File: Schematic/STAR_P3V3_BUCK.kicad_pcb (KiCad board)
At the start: 2 copper layers, 70.1 x 70 mm, 19 parts, among them J1 1017491, J2 6120XX21621_61200621621, J3 6120XX21621_61200821621, U1 TLV62569ADRLR

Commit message: V1.2.0
Lots Of changes, need help with screw holes
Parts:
- moved H4 12.5 mm to (190.0, 84.8)
- moved C8 10.7 mm to (171.2, 69.8), turned to -90 degrees
- moved H3 9.63 mm to (143.9, 84.8)
- moved C4 9.16 mm to (148.6, 71.0), turned to 90 degrees
- moved H2 8.99 mm to (190.0, 41.3)
- moved C7 8.58 mm to (168.4, 69.8), turned to 90 degrees
- moved J3 8.41 mm to (181.1, 72.8)
- moved R2 7.62 mm to (164.7, 64.6)
- moved C1 7.58 mm to (156.7, 71.0), turned to 90 degrees
- moved C6 5.78 mm to (173.8, 69.8), turned to 90 degrees
- moved L1 5.47 mm to (167.9, 76.4)
- moved H1 4.71 mm to (143.3, 41.3)
- moved J2 3.94 mm to (178.0, 57.5)
- moved C5 2.87 mm to (159.9, 71.0), turned to 90 degrees
- moved R1 2.30 mm to (164.7, 66.3), turned to 0 degrees
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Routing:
- net GND: track 43.8 -> 19.9 mm, vias 13 -> 12
- net /P3V3_BUCK: track 36.5 -> 22.4 mm, vias 7 -> 2
- net Net-(U1-SW): track 3.00 -> 5.57 mm
- net Net-(U1-FB): track 3.01 -> 4.44 mm
- net /P5V0_BUCK: track 13.1 -> 12.0 mm, vias 7 -> 5
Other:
- board size 70.1 x 70 mm -> 43.3 x 40.1 mm

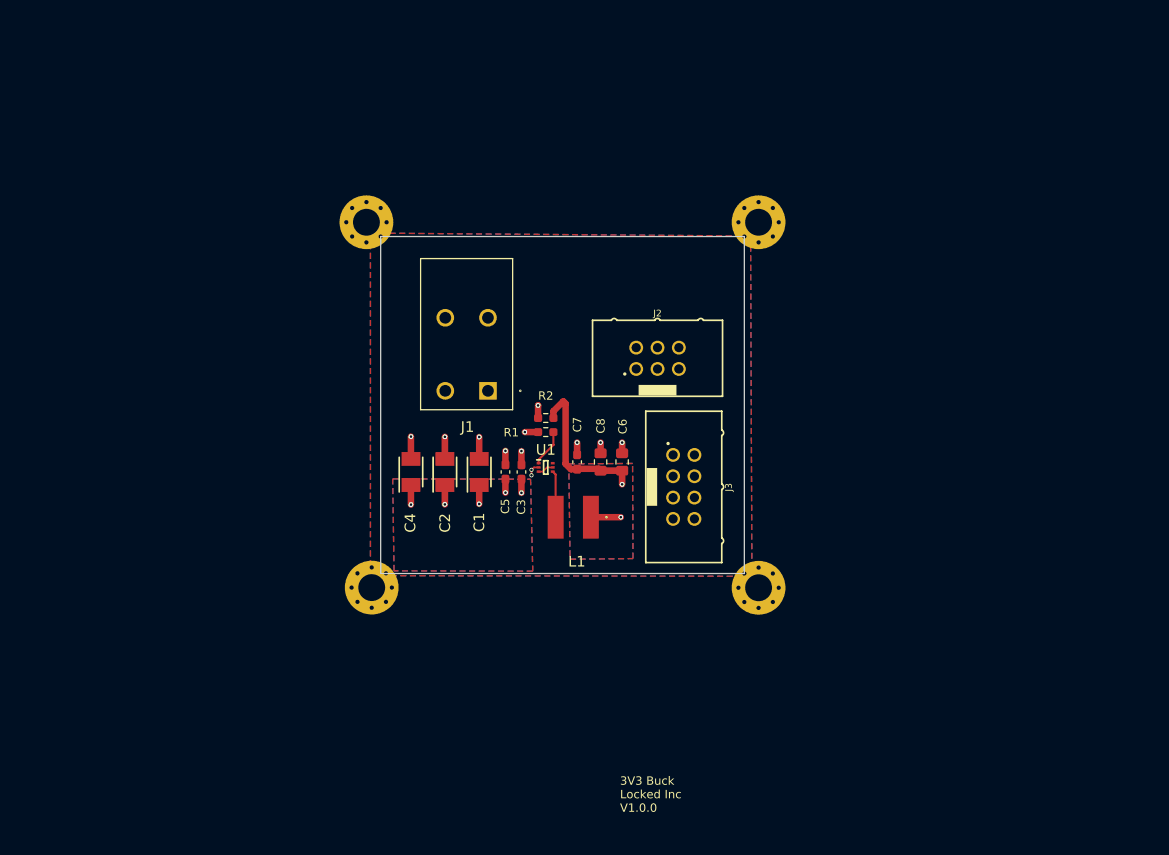
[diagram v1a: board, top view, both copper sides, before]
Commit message: Updated PCB
Added a polypour for the switching
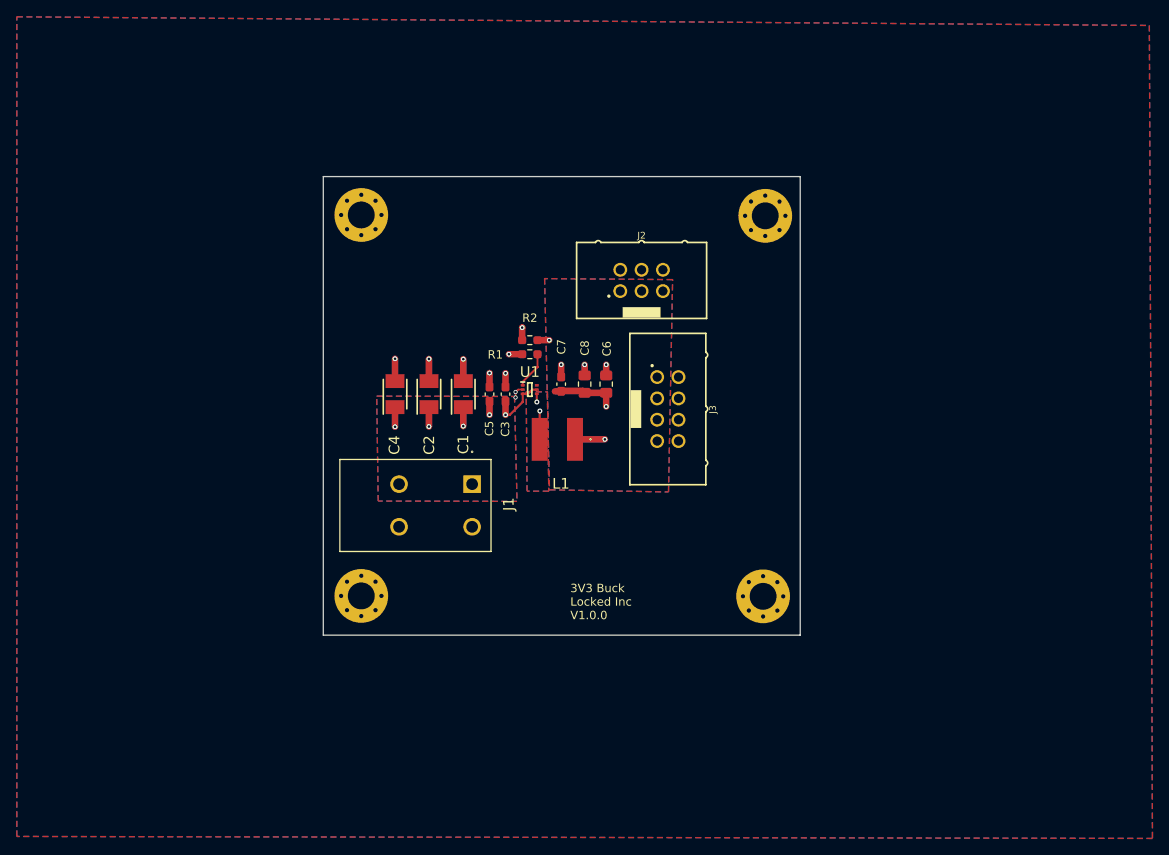
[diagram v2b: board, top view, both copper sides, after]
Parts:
- moved J1 11.3 mm to (155.9, 72.5), turned to -90 degrees
- moved C3 9.46 mm to (159.9, 61.8)
- moved J2 9.46 mm to (176.1, 48.2)
- moved U1 9.46 mm to (162.8, 61.2)
- moved L1 9.46 mm to (166.0, 67.2)
- moved C1 9.46 mm to (154.8, 61.8)
- moved C5 9.46 mm to (158.0, 61.8)
- moved C6 9.46 mm to (171.9, 60.6)
- moved J3 9.46 mm to (179.2, 63.6)
- moved R1 9.46 mm to (162.8, 57.0)
- moved R2 9.46 mm to (162.8, 55.3)
- moved C2 9.46 mm to (150.8, 61.8)
- moved C4 9.46 mm to (146.7, 61.8)
- moved C7 9.46 mm to (166.5, 60.6)
- moved C8 9.46 mm to (169.3, 60.6)
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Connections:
- net Net-(U1-SW) renamed /Switch
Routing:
- net /P3V3_BUCK: track 22.4 -> 12.8 mm, vias 2 -> 3
- net /P5V0_BUCK: track 12.0 -> 15.7 mm
- net /Switch: track 5.57 -> 4.37 mm, vias 0 -> 2
- added copper zone on B.Cu, net /Switch
- added copper zone on F.Cu, net /Switch
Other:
- board size 43.3 x 40.1 mm -> 56.8 x 54.6 mm

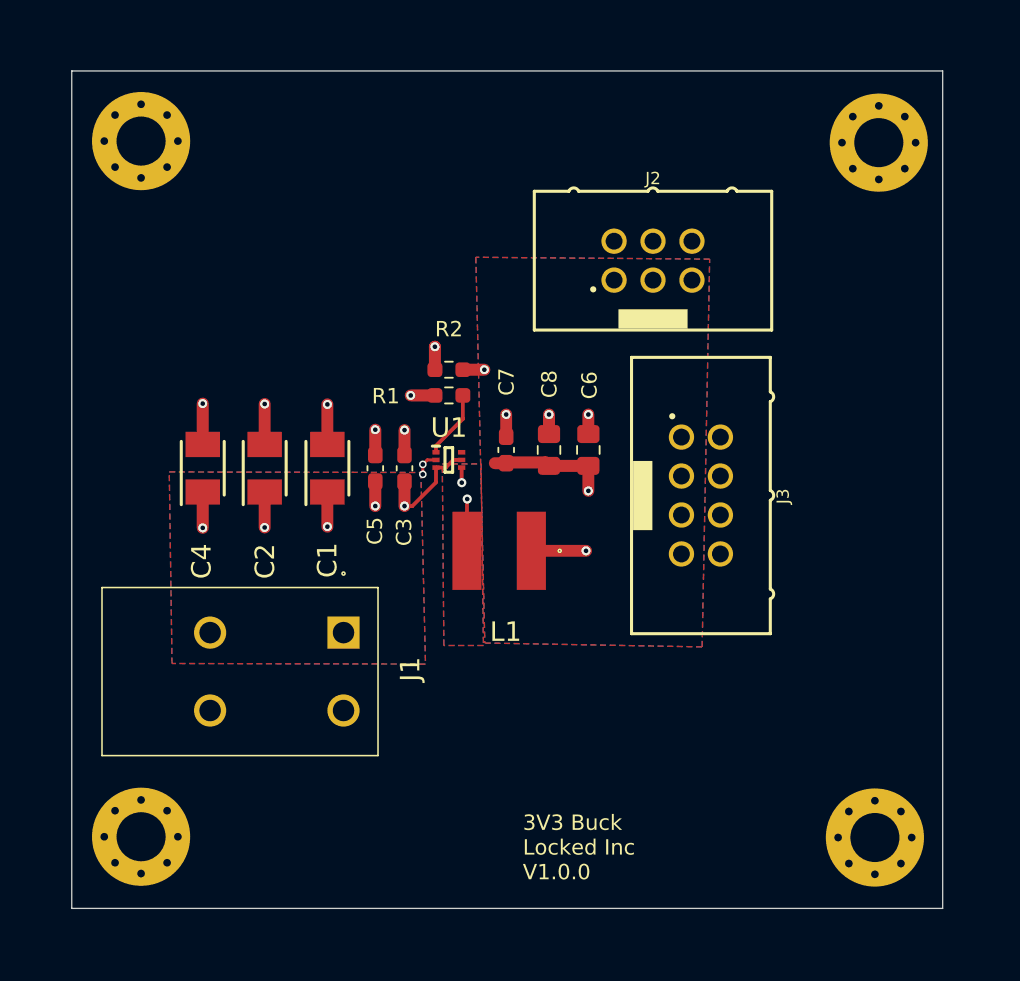
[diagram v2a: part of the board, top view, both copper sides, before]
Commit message: Push PCB
Fixed the mounting holes and took out uneccesarry vias
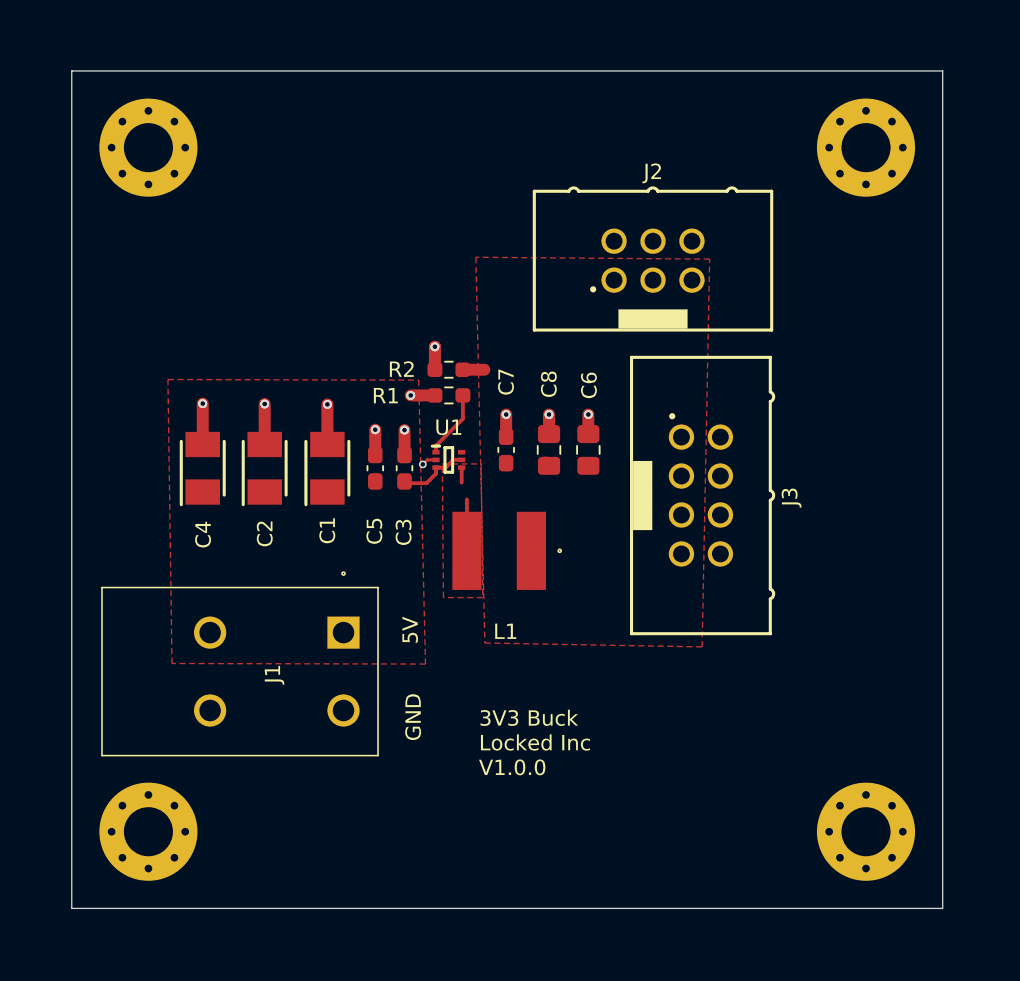
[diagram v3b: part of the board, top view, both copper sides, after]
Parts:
- moved H2 0.90 mm to (190.0, 40.9)
- moved H4 0.69 mm to (190.0, 85.5)
- moved H1 0.64 mm to (143.2, 40.9)
- moved H3 0.58 mm to (143.2, 85.5)
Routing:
- net /P3V3_BUCK: track 12.8 -> 1.77 mm, vias 3 -> 0
- net /P5V0_BUCK: track 15.7 -> 4.63 mm, vias 5 -> 0
- net GND: track 19.9 -> 19.2 mm, vias 12 -> 11
- net /Switch: track 4.37 -> 4.34 mm, vias 2 -> 0
- removed copper zone on B.Cu, net /P3V3_BUCK
- removed copper zone on B.Cu, net /P5V0_BUCK
- removed copper zone on B.Cu, net /Switch
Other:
- board text added: "5V"
- board text added: "GND"

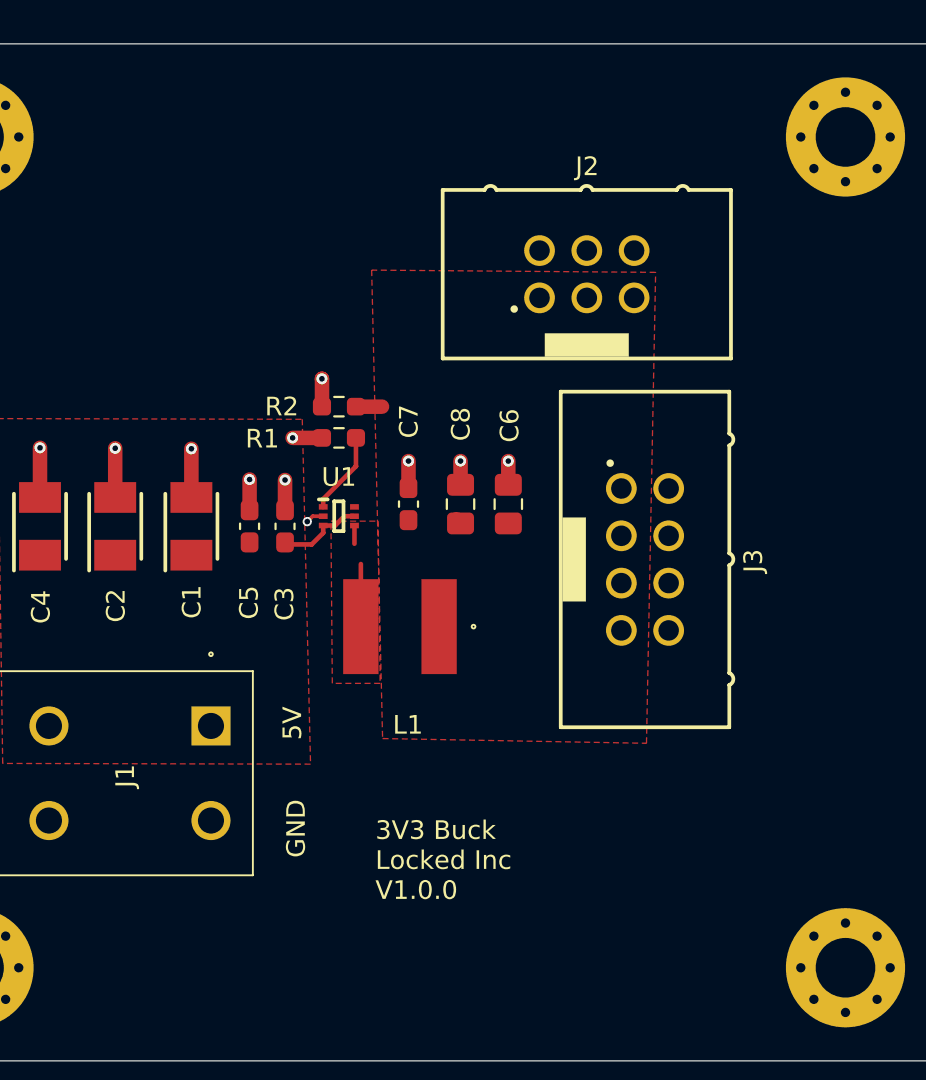
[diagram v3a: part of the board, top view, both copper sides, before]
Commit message: fixed the silk screen
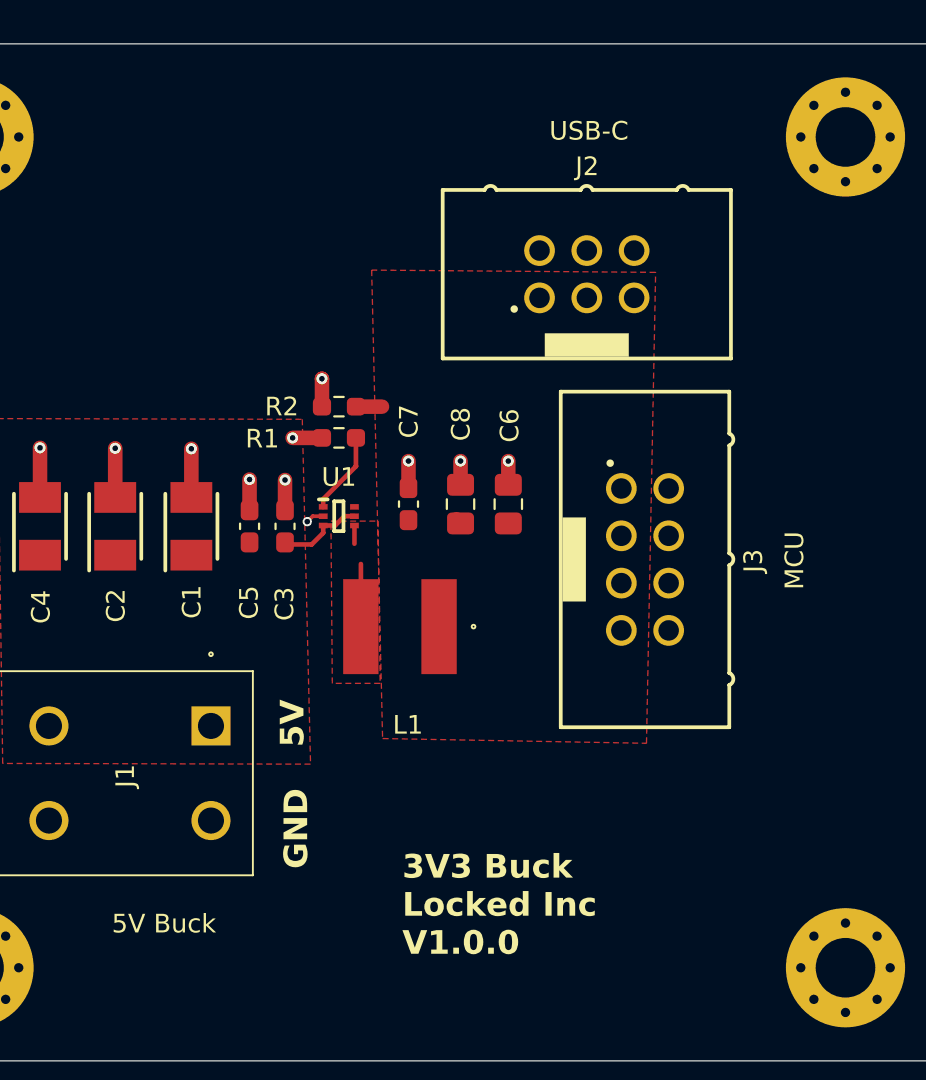
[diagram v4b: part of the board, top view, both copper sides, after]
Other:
- board text added: "5V Buck"
- board text added: "MCU"
- board text added: "USB-C"
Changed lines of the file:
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@@
 		(layer "Edge.Cuts")
+	)
+	(gr_text "5V Buck"
+		(at 150.57 83.7 0)
+		(layer "F.SilkS")
+		(effects
+			(font
+				(size 1 1)
+				(thickness 0.15)
+			)
+			(justify left bottom)
+		)
 	)
 	(gr_text "5V"
@@
 		(effects
 			(font
-				(size 1 1)
-				(thickness 0.15)
+				(size 1.27 1.27)
+				(thickness 0.254)
+				(bold yes)
 			)
 		)
 	)
 	(gr_text "3V3 Buck\nLocked Inc\nV1.0.0"
-		(at 164.725 81.9 0)
+		(at 166.17 84.88 0)
+		(layer "F.SilkS")
+		(effects
+			(font
+				(size 1.27 1.27)
+				(thickness 0.254)
+				(bold yes)
+			)
+			(justify left bottom)
+		)
+	)
+	(gr_text "MCU"
+		(at 187.82 65.18 90)
 		(layer "F.SilkS")
 		(effects
@@
 		(effects
 			(font
+				(size 1.27 1.27)
+				(thickness 0.254)
+				(bold yes)
+			)
+		)
+	)
+	(gr_text "USB-C"
+		(at 174.06 41.13 0)
+		(layer "F.SilkS")
+		(effects
+			(font
 				(size 1 1)
 				(thickness 0.15)
 			)
+			(justify left bottom)
 		)
 	)
